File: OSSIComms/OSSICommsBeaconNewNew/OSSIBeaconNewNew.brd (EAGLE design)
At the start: 92 x 92 mm, 116 parts, among them Q1 NX-3215, U1 MAX890L, U10 MSP430F2132, U2 ADL5530, U3 NC7SZ04, U4 ADF7012, U5 OPA2347, U6 MAX890L, U7 MAX6369, U8 MCP1700_SOT23, U9 TPS3838, X1 ESQ-126-38-G-D, X2 RFCON-MCX-R/A, X3 5268-02, X4 JTAG10PINMINI-H, X5 5268-03, X7 P-PAD-S, X8 P-PAD-S

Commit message: beta 1 release
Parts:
- moved X6 2.54 mm to (88.9, 28.6)
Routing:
- net BEACON_SDA: track 58.6 -> 59.4 mm
- net BEACON_SCL: track 56.5 -> 57.3 mm
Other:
- outline, holes or cut-outs redrawn
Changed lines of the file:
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@@
 <setting verticaltext="up"/>
 </settings>
-<grid distance="1.27" unitdist="mm" unit="mm" style="lines" multiple="1" display="yes" altdistance="0.0125" altunitdist="inch" altunit="inch"/>
+<grid distance="1" unitdist="mm" unit="mm" style="lines" multiple="1" display="yes" altdistance="0.025" altunitdist="inch" altunit="inch"/>
 <layers>
 <layer number="1" name="Top" color="4" fill="1" visible="yes" active="yes"/>
@@
 <layer number="27" name="tValues" color="7" fill="1" visible="no" active="yes"/>
 <layer number="28" name="bValues" color="7" fill="1" visible="no" active="yes"/>
-<layer number="29" name="tStop" color="7" fill="3" visible="yes" active="yes"/>
+<layer number="29" name="tStop" color="7" fill="3" visible="no" active="yes"/>
 <layer number="30" name="bStop" color="7" fill="6" visible="no" active="yes"/>
 <layer number="31" name="tCream" color="7" fill="4" visible="no" active="yes"/>
@@
 <wire x1="3" y1="0" x2="89" y2="0" width="0" layer="20"/>
 <wire x1="89" y1="0" x2="92" y2="3" width="0" layer="20" curve="90"/>
-<wire x1="92" y1="3" x2="92" y2="89" width="0" layer="20"/>
+<wire x1="92" y1="3" x2="92" y2="36" width="0" layer="20"/>
+<wire x1="92" y1="56" x2="92" y2="89" width="0" layer="20"/>
 <wire x1="92" y1="89" x2="89" y2="92" width="0" layer="20" curve="90"/>
 <wire x1="79" y1="90" x2="79" y2="91" width="0" layer="20"/>
@@
 <wire x1="16" y1="87" x2="76" y2="87" width="0" layer="20"/>
 <wire x1="76" y1="87" x2="79" y2="90" width="0" layer="20" curve="90"/>
-<text x="89.535" y="39.6875" size="1.27" layer="1" font="vector" rot="R90">SDA</text>
-<text x="89.535" y="44.45" size="1.27" layer="1" font="vector" rot="R90">SCL</text>
-<text x="89.535" y="48.895" size="1.27" layer="1" font="vector" rot="R90">GND</text>
-<text x="89.535" y="48.895" size="1.27" layer="29" font="vector" rot="R90">GND</text>
-<text x="89.535" y="44.45" size="1.27" layer="29" font="vector" rot="R90">SCL</text>
-<text x="89.535" y="39.6875" size="1.27" layer="29" font="vector" rot="R90">SDA</text>
+<text x="89.535" y="13.0175" size="1.27" layer="1" font="vector" rot="R90">SDA</text>
+<text x="89.535" y="17.78" size="1.27" layer="1" font="vector" rot="R90">SCL</text>
+<text x="89.535" y="22.225" size="1.27" layer="1" font="vector" rot="R90">GND</text>
+<text x="89.535" y="22.225" size="1.27" layer="29" font="vector" rot="R90">GND</text>
+<text x="89.535" y="17.78" size="1.27" layer="29" font="vector" rot="R90">SCL</text>
+<text x="89.535" y="13.0175" size="1.27" layer="29" font="vector" rot="R90">SDA</text>
 <text x="11.43" y="71.12" size="1.778" layer="1" font="vector" rot="SR270">G.O.D.Sat</text>
 <text x="6.35" y="71.12" size="1.778" layer="1" font="vector" rot="SR270">CW Beacon</text>
@@
 <text x="29.21" y="55.245" size="1.27" layer="29" font="vector" rot="R90">P3.0</text>
 <text x="29.21" y="55.245" size="1.27" layer="1" font="vector" rot="R90">P3.0</text>
+<wire x1="90" y1="38" x2="88" y2="40" width="0" layer="20" curve="-90"/>
+<wire x1="88" y1="40" x2="88" y2="52" width="0" layer="20"/>
+<wire x1="88" y1="52" x2="90" y2="54" width="0" layer="20" curve="-90"/>
+<wire x1="92" y1="36" x2="92" y2="37" width="0" layer="20"/>
+<wire x1="92" y1="37" x2="91" y2="38" width="0" layer="20" curve="90"/>
+<wire x1="91" y1="38" x2="90" y2="38" width="0" layer="20"/>
+<wire x1="92" y1="56" x2="92" y2="55" width="0" layer="20"/>
+<wire x1="92" y1="55" x2="91" y2="54" width="0" layer="20" curve="-90"/>
+<wire x1="91" y1="54" x2="90" y2="54" width="0" layer="20"/>
 </plain>
 <attributes>
@@
 <element name="R27" library="OSSI" package="R0603(1608)" value="4.7k" x="59.69" y="43.18"/>
 <element name="R26" library="OSSI" package="R0603(1608)" value="4.7k" x="59.69" y="41.91"/>
-<element name="X6" library="OSSI" package="1X03" value="" x="88.9" y="31.115" rot="R90"/>
+<element name="X6" library="OSSI" package="1X03" value="" x="88.9" y="28.575" rot="R90"/>
 <element name="R39" library="OSSI" package="WSL1206" value="511" x="8.89" y="78.105" rot="R90"/>
 <element name="C43" library="OSSI" package="C0805(2012)" value="" x="6.35" y="78.105" rot="R270"/>
@@
 <vertex x="12.7" y="0"/>
 <vertex x="80.01" y="0"/>
-<vertex x="80.01" y="31.75"/>
+<vertex x="80.01" y="30.75"/>
+<vertex x="79.01" y="31.75"/>
 </polygon>
 <polygon width="0.254" layer="1" thermals="no">
@@
 <vertex x="77.47" y="13.335"/>
 <vertex x="77.47" y="31.75"/>
-<vertex x="80.3275" y="31.75"/>
+<vertex x="79.3275" y="31.75"/>
+<vertex x="80.3275" y="30.75"/>
 <vertex x="80.3275" y="0"/>
 <vertex x="12.7" y="0"/>
@@
 <wire x1="81.28" y1="33.48" x2="82.73" y2="32.03" width="0.4064" layer="16"/>
 <contactref element="X6" pad="2"/>
-<wire x1="86.6775" y1="33.3375" x2="84.1375" y2="33.3375" width="0.4064" layer="1"/>
+<wire x1="85.4075" y1="33.3375" x2="84.1375" y2="33.3375" width="0.4064" layer="1"/>
 <wire x1="84.1375" y1="33.3375" x2="82.8675" y2="32.0675" width="0.4064" layer="1"/>
 <wire x1="82.8675" y1="32.0675" x2="82.7675" y2="32.0675" width="0.4064" layer="1"/>
 <wire x1="82.7675" y1="32.0675" x2="82.73" y2="32.03" width="0.4064" layer="1"/>
-<wire x1="86.6775" y1="33.3375" x2="88.5825" y2="33.3375" width="0.4064" layer="1"/>
-<wire x1="88.5825" y1="33.3375" x2="88.9" y2="33.655" width="0.4064" layer="1"/>
+<wire x1="85.4075" y1="33.3375" x2="86.0425" y2="33.3375" width="0.4064" layer="1"/>
+<wire x1="86.0425" y1="33.3375" x2="87.63" y2="31.75" width="0.4064" layer="1"/>
+<wire x1="87.63" y1="31.75" x2="88.265" y2="31.115" width="0.4064" layer="1"/>
+<wire x1="88.265" y1="31.115" x2="88.9" y2="31.115" width="0.4064" layer="1"/>
 </signal>
 <signal name="BEACON_SDA">
@@
 <wire x1="82.73" y1="29.49" x2="82.83" y2="29.49" width="0.4064" layer="1"/>
 <wire x1="82.83" y1="29.49" x2="84.1375" y2="30.7975" width="0.4064" layer="1"/>
-<wire x1="84.1375" y1="30.7975" x2="88.5825" y2="30.7975" width="0.4064" layer="1"/>
-<wire x1="88.5825" y1="30.7975" x2="88.9" y2="31.115" width="0.4064" layer="1"/>
+<wire x1="84.1375" y1="30.7975" x2="86.0425" y2="30.7975" width="0.4064" layer="1"/>
+<wire x1="86.0425" y1="30.7975" x2="87.63" y2="29.21" width="0.4064" layer="1"/>
+<wire x1="87.63" y1="29.21" x2="88.265" y2="28.575" width="0.4064" layer="1"/>
+<wire x1="88.265" y1="28.575" x2="88.9" y2="28.575" width="0.4064" layer="1"/>
 </signal>
 <signal name="COMMS_SDA">

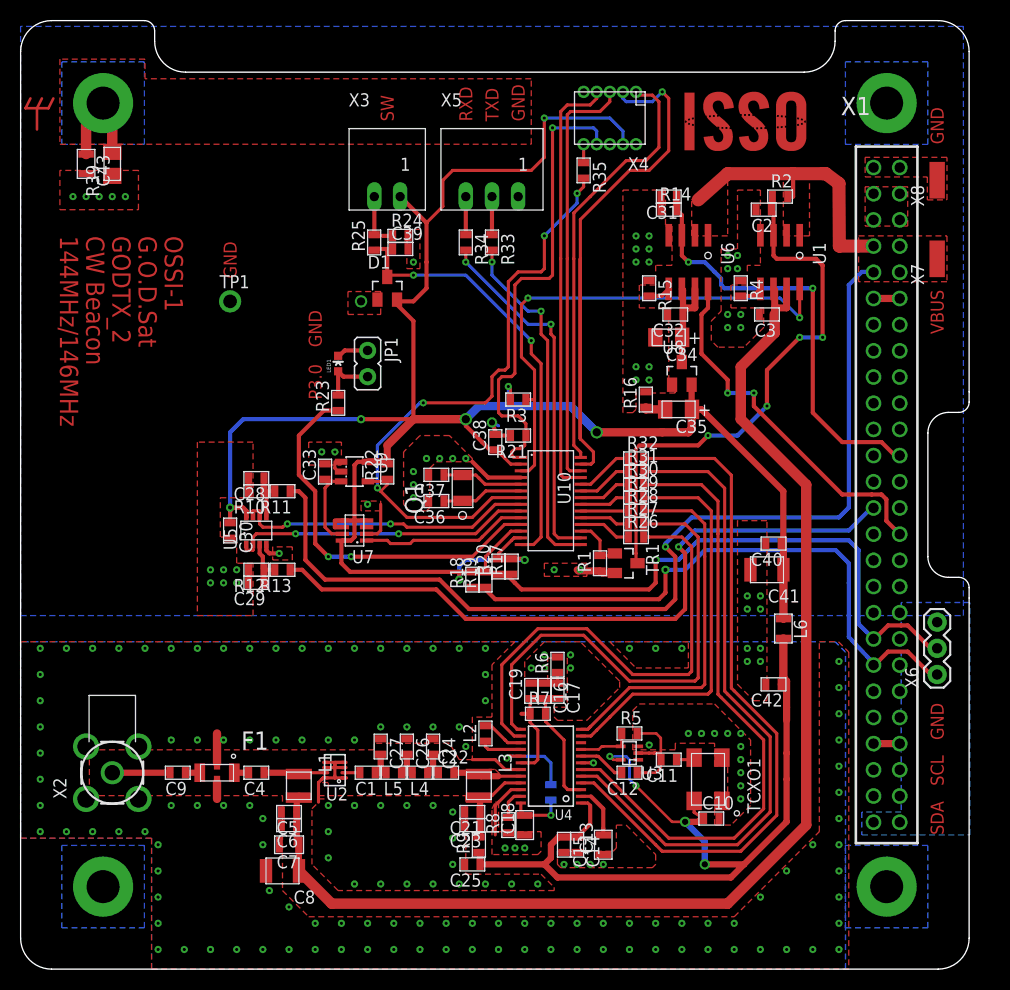
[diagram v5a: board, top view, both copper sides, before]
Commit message: schematics renumbered
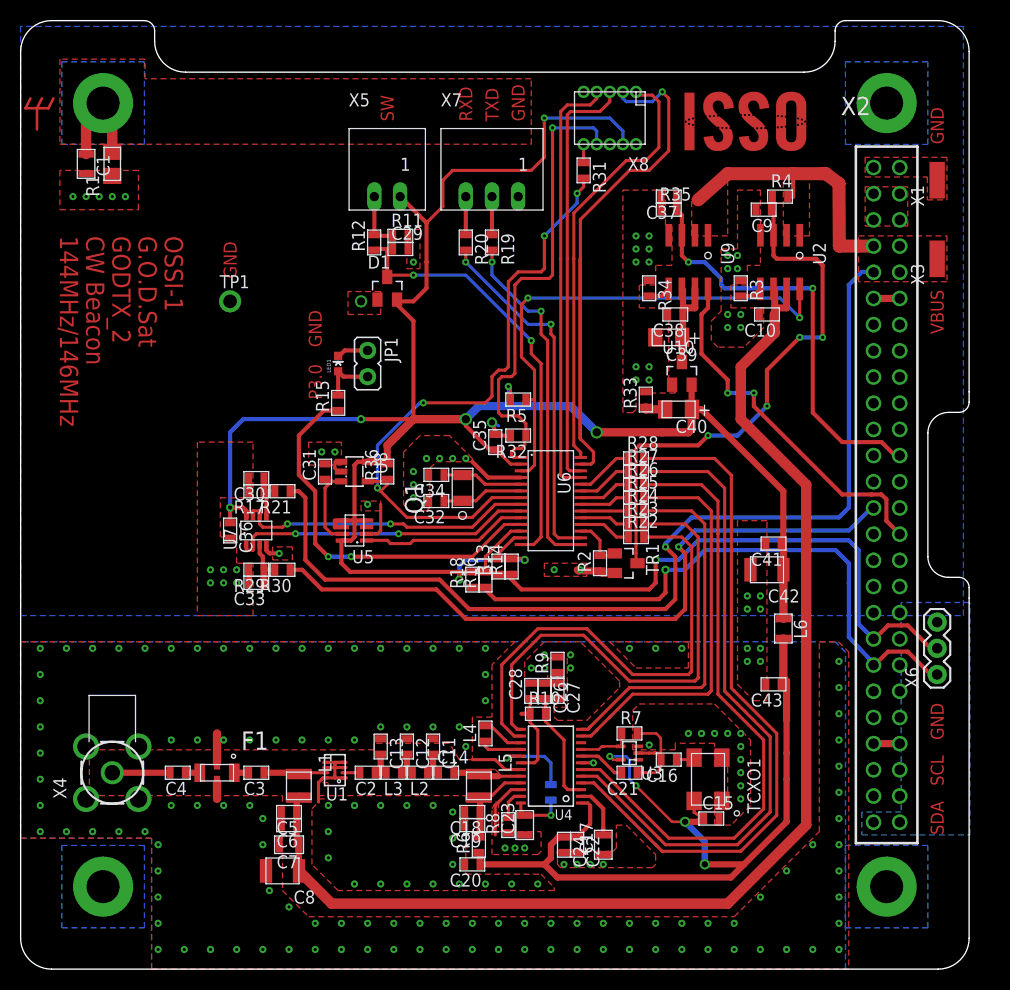
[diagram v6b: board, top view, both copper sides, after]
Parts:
- removed R39: 511, OSSI:WSL1206
- added R36: 100k, OSSI:R0603(1608)
- C1: value 10nF -> (none); device OSSI:C0603(1608) -> OSSI:C0805(2012)
- C10: value 10nF -> 100nF
- C11: value 1nF -> 22pF
- C12: value DNP -> 22pF
- C13: value 2.2uF, 0805 -> 22pF; device OSSI:C0805(2012) -> OSSI:C0603(1608)
- C14: value 100pF -> 1nF
- C15: value 1uF,0603 -> 10nF
- C16: value 68pF -> 1nF
- C17: value 1000pF -> 2.2uF, 0805; device OSSI:C0603(1608) -> OSSI:C0805(2012)
- C18: value 1uF 0805 -> 100pF; device OSSI:C0805(2012) -> OSSI:C0603(1608)
- C19: value 22pF -> 1uF
- C2: value 1uF -> 10nF
- C20: value 22nF -> (none)
- C21: value 100pF -> DNP
- C22: value 1nF -> 100pF
- C23: value 1uF -> 1uF 0805; device OSSI:C0603(1608) -> OSSI:C0805(2012)
- C24: value 22pF -> 1uF,0603
- C25: value (none) -> 22nF
- C26: value 22pF -> 68pF
- C27: value 22pF -> 1000pF
- C28: value TBD -> 22pF
- C29: value TBD -> 100nF
- C3: value 100nF -> 10nF
- C30, C33: value 100nF -> TBD
- C31: value 1uF -> 100nF
- C32: value 100nF -> 12.5pF
- C34: value 10uF, LDO Tantal 16V -> 12.5pF; device OSSI:C1206(3216)-A -> OSSI:C0603(1608)
- C35: value 10uF, LDO Tantal 16V -> 100nF; device OSSI:C1206(3216)-A -> OSSI:C0603(1608)
- C36: value 12.5pF -> 100nF
- C37: value 12.5pF -> 1uF
- C39: value 100nF -> 10uF, LDO Tantal 16V; device OSSI:C0603(1608) -> OSSI:C1206(3216)-A
- C4: value 10nF -> (none)
- C40: value 10nF -> 10uF, LDO Tantal 16V; device OSSI:C0603(1608) -> OSSI:C1206(3216)-A
- C41: value 22uF,1210 -> 10nF; device OSSI:C1210-GCM32 -> OSSI:C0603(1608)
- C42: value 100nF -> 22uF,1210; device OSSI:C0603(1608) -> OSSI:C1210-GCM32
- C43: value (none) -> 100nF; device OSSI:C0805(2012) -> OSSI:C0603(1608)
- C9: value (none) -> 1uF
- L2: value 10nH -> 68nH
- L3: value 470nH, 1008 size -> 68nH; device OSSI:L1008(2520) -> OSSI:L0603(1608)
- L4: value 68nH -> 10nH
- L5: value 68nH -> 470nH, 1008 size; device OSSI:L0603(1608) -> OSSI:L1008(2520)
- R1: value 100k -> 511; device OSSI:R0603(1608) -> OSSI:WSL1206
- R10: value 100k -> 5.1k
- R11: value 100k -> 47k
- R12, R22: value 100k -> 4.7k
- R13: value 100k -> 250
- R14: value 100k -> 10k
- R15: value 23.7k -> 1k
- R16: value 0 -> 250
- R17: value 10k -> 100k
- R19, R20: value 250 -> 4.7k
- R21, R29, R30, R35: value 4.7k -> 100k
- R23: value 1k -> 4.7k
- R24: value 47k -> 4.7k
- R3: value 100k -> 6.2k
- R33: value 4.7k -> 0
- R34: value 4.7k -> 23.7k
- R4: value 6.2k -> 100k
- R5: value 1M -> 100k
- R6: value 2.4k -> 0
- R7: value 5.1k -> 1M
- R9: value 0 -> 2.4k
- U1: value MAX890L -> ADL5530; device OSSI:SO8 -> OSSI:LFCSP8_CP
- U10: value MSP430F2132 -> MCP1700_SOT23; device OSSI:PW28 -> OSSI:SOT23
- U2: value ADL5530 -> MAX890L; device OSSI:LFCSP8_CP -> OSSI:SO8
- U5: value OPA2347 -> MAX6369; device OSSI:SOT23-8DCN -> OSSI:SOT23-8
- U6: value MAX890L -> MSP430F2132; device OSSI:SO8 -> OSSI:PW28
- U7: value MAX6369 -> OPA2347; device OSSI:SOT23-8 -> OSSI:SOT23-8DCN
- U8: value MCP1700_SOT23 -> TPS3838; device OSSI:SOT23 -> OSSI:SOT23-5DBV
- U9: value TPS3838 -> MAX890L; device OSSI:SOT23-5DBV -> OSSI:SO8
- X1: value ESQ-126-38-G-D -> P-PAD-S; device OSSI:ESQ-126-XX-X-D -> OSSI:P-PAD-S
- X2: value RFCON-MCX-R/A -> ESQ-126-38-G-D; device OSSI:MCX-R/A -> OSSI:ESQ-126-XX-X-D
- X3: value 5268-02 -> P-PAD-S; device OSSI:5628-02 -> OSSI:P-PAD-S
- X4: value JTAG10PINMINI-H -> RFCON-MCX-R/A; device OSSI:M50-3200545 -> OSSI:MCX-R/A
- X5: value 5268-03 -> 5268-02; device OSSI:5268-03 -> OSSI:5628-02
- X7: value P-PAD-S -> 5268-03; device OSSI:P-PAD-S -> OSSI:5268-03
- X8: value P-PAD-S -> JTAG10PINMINI-H; device OSSI:P-PAD-S -> OSSI:M50-3200545
- moved C43 83.6 mm to (73.0, 27.6), turned to 180 degrees
- moved X2 79.8 mm to (84.0, 46.0), turned to 0 degrees
- moved X4 79.8 mm to (8.89, 19.1), turned to 90 degrees
- moved C9 78.8 mm to (72.1, 73.7)
- moved C2 66.8 mm to (33.7, 19.1)
- moved C3 66.6 mm to (22.9, 19.1)
- moved U1 65.5 mm to (30.5, 19.3)
- moved U2 65.5 mm to (73.7, 68.6)
- moved C1 65.1 mm to (6.35, 78.1), turned to 270 degrees
- moved R1 61.1 mm to (8.89, 78.1)
- moved X3 53.7 mm to (88.9, 68.9), turned to 90 degrees
- moved C10 49.2 mm to (72.4, 63.5), turned to 180 degrees
- moved X7 43.6 mm to (45.7, 74.9), turned to 0 degrees
- moved C31 42.7 mm to (29.5, 48.3), turned to 90 degrees
- moved R2 39.6 mm to (56.2, 39.4), turned to 90 degrees
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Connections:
- net 3.3VBEACON: now also C36.1, C41.1, C42.P$1, R14.2, R36.2, R5.2, U5.4, U5.5, U5.6, U6.2, U8.5, X5.1, X8.4; no longer C30.1, C38.1, C41.P$1, R17.2, R22.2, R3.2, U7.4, U7.5, U7.6, U8.2, U9.5, X3.1, X4.4
- net 3.3VOBC: now also X2.45, X2.46; no longer X1.45, X1.46
- net ADC0: now also U6.8, U7.6, U7.7; no longer U10.8, U5.6, U5.7
- net ADC1: now also U6.9, U7.1, U7.2; no longer U10.9, U5.1, U5.2
- net ANT_DEPLOY1: now also X2.19; no longer X1.19
- net ANT_DEPLOY2: now also X2.20; no longer X1.20
- net BAT_-CHRG: now also X2.42; no longer X1.42
- net BAT_-FAULT: now also X2.44; no longer X1.44
- net BAT_-ON: now also X2.38; no longer X1.38
- net BAT_TEMP: now also X2.47; no longer X1.47
- net BEACON_-FAULT: now also U9.8, X2.30; no longer U6.8, X1.30
- net BEACON_CE: now also R22.2; no longer R26.2
- net BEACON_CWCONTROL: now also R11.1, R12.2, X5.2; no longer R24.1, R25.2, X3.2
- net BEACON_DATA: now also R28.2; no longer R32.2
- net BEACON_MUXOUT: now also R26.2; no longer R30.2
- net BEACON_OFF: now also C37.1, R35.2, U9.3, X2.24; no longer C31.1, R14.2, U6.3, X1.24
- net BEACON_RFOUT: now also C13.2, C2.1, L3.2; no longer C1.1, C27.2, L5.2
- net BEACON_SCL: now also R13.1, R14.1, X2.37; no longer R17.1, R20.1, X1.37
- net BEACON_SCLK: now also R25.2; no longer R29.2
- net BEACON_SDA: now also R16.1, X2.39; no longer R19.1, X1.39
- net BEACON_SDATA: now also R24.2; no longer R28.2
- net BEACON_SLE: now also R23.2; no longer R27.2
- net BEACON_TXCLK: now also R27.2; no longer R31.2
- net BEACON_WDT_RST: now also C31.1, U5.7, U8.3; no longer C33.1, U7.7, U9.3
- net BUS_CS: now also R30.1, X2.27; no longer R13.1, X1.27
- net COMMS_-FAULT: now also X2.32; no longer X1.32
- net COMMS_OFF: now also X2.25; no longer X1.25
- net COMMS_SCL: now also X2.41; no longer X1.41
- net COMMS_SDA: now also X2.43; no longer X1.43
- net GND: now also C1.2, C11.1, C12.1, C17.1, C18.2, C20.2, C22.2, C23.1, C24.2, C35.2, C41.2, C42.P$2, C9.2, R1.P$1, R11.2, R17.2, R2.1, R29.2, R3.1, R32.2, R33.2, R34.1, R35.1, R9.2, U1.1, U1.3, U1.5, U1.6, U1.8, U10.1, U5.2, U7.4, U8.2, U9.4, X2.1, X2.51, X2.52, X4.2, X4.3, X4.4, X4.5, X7.1, X8.9; no longer C14.2, C16.1, C18.1, C2.2, C21.2, C23.2, C24.1, C25.2, C27.1, C3.2, C40.2, C41.P$2, C42.2, R1.1, R10.2, R12.2, R14.1, R15.1, R16.2, R21.2, R24.2, R39.P$1, R4.1, R6.2, U10.4, U2.1, U2.3, U2.5, U2.6, U2.8, U5.4, U7.2, U9.1, U9.2, X1.2, X1.51, X1.52, X2.3, X2.4, X2.5, X4.9, X5.1, X8.1
- net LED_-FAULT: now also X2.28; no longer X1.28
- net LED_OFF: now also X2.23; no longer X1.23
- net LED_SCL: now also X2.33; no longer X1.33
- net LED_SDA: now also X2.35; no longer X1.35
- net N$1: now also R15.1, U6.11; no longer R23.1, U10.11
- net N$10: now also R13.2, U6.13; no longer R20.2, U10.13
- net N$11: now also R20.2, U6.16; no longer R34.2, U10.16
- net N$12: now also U5.1, U6.10; no longer U10.10, U7.1
- net N$13: now also C29.1, R12.1, U6.14; no longer C39.1, R25.1, U10.14
- net N$14: now also L4.1; no longer L2.1
- net N$15: now also L4.2; no longer L2.2
- net N$16: now also C23.2, C25.1; no longer C18.2, C20.1
- net N$17: now also C25.2; no longer C20.2
- net N$19: now also C9.1, R4.1, U2.3; no longer C2.1, R2.1, U1.3
- net N$2: now also U6.27, X8.3; no longer U10.27, X4.3
- net N$20: now also C27.1, R9.1; no longer C17.1, R6.1
- net N$21: now also R3.2, U2.5; no longer R4.2, U1.5
- net N$22: now also C30.1, R17.1, R21.2, U7.5; no longer C28.1, R10.1, R11.2, U5.5
- net N$23: now also C14.2, L5.P$2; no longer C22.2, L3.P$2
- net N$24: now also C28.1, R10.1; no longer C19.1, R7.1
- net N$25: now also C17.2; no longer C13.2
- net N$26: now also C26.2, C27.2, R10.2; no longer C16.2, C17.2, R7.2
- net N$27: now also C18.1, C19.1, L5.P$1, R6.2; no longer C21.1, C23.1, L3.P$1, R9.2
- net N$28: now also C2.2, U1.2; no longer C1.2, U2.2
- net N$29: now also C11.2, C14.1, L2.1; no longer C22.1, C24.2, L4.1
- net N$3: now also U6.26, X8.5; no longer U10.26, X4.5
- net N$30: now also C3.1, U1.7; no longer C4.1, U2.7
- net N$31: now also R31.1, X8.10; no longer R35.1, X4.10
- net N$32: now also R34.2, U9.5; no longer R15.2, U6.5
- net N$33: now also C33.1, R29.1, R30.2, U7.3; no longer C29.1, R12.1, R13.2, U5.3
- net N$34: now also C3.2; no longer C4.2
- net N$35: now also C4.1; no longer C9.1
- net N$36: now also C12.2, L2.2, L3.1; no longer C26.2, L4.2, L5.1
- net N$37: now also C4.2, X4.1; no longer C9.2, X2.1
- net N$38: now also C16.2, C21.1, R7.2; no longer C11.2, C12.1, R5.2
- net N$39: now also R19.2, U6.15; no longer R33.2, U10.15
- net N$4: now also U6.25, X8.7; no longer U10.25, X4.7
- net N$40: now also C40.2, R33.1; no longer C35.2, R16.1
- net N$41: now also R28.1, U6.24; no longer R32.1, U10.24
- net N$42: now also R27.1, U6.23; no longer R31.1, U10.23
- net N$43: now also R26.1, U6.22; no longer R30.1, U10.22
- net N$44: now also R25.1, U6.21; no longer R29.1, U10.21
- net N$45: now also R24.1, U6.20; no longer R28.1, U10.20
- net N$46: now also R23.1, U6.19; no longer R27.1, U10.19
- net N$47: now also R22.1, U6.18; no longer R26.1, U10.18
- net N$5: now also C34.1, U6.5; no longer C37.1, U10.5
- net N$6: now also C32.1, U6.6; no longer C36.1, U10.6
- net N$666: now also C38.1, C39.1, U10.3, U9.6, U9.7; no longer C32.1, C34.1, U6.6, U6.7, U8.3
- net N$69: now also C16.1; no longer C11.1
- net N$7: now also R15.2; no longer R23.2
- net N$8: now also U6.28, X8.1; no longer U10.28, X4.1
- net N$9: now also R16.2, U6.12; no longer R19.2, U10.12
- net OBC_-FAULT: now also X2.34; no longer X1.34
- net OBC_OFF: now also X2.26; no longer X1.26
- net OSC1: now also C21.2; no longer C12.2
- net OSC2: now also R7.1; no longer R5.1
- net PANELTEMP_SCL: now also X2.29; no longer X1.29
- net PANELTEMP_SDA: now also X2.31; no longer X1.31
- net PA_-FAULT: now also R5.1, U2.8, U6.3; no longer R3.1, U1.8, U10.3
- net PA_ON: now also R2.2, U6.17; no longer R1.2, U10.17
- net RESETBEACON: now also R31.2, R36.1, U6.7, U8.4; no longer R22.1, R35.2, U10.7, U9.4
- net RXD: now also R20.1, X7.3; no longer R34.1, X5.3
- net SCCHG_EN: now also X2.21; no longer X1.21
- net SCOUT_-PG: now also X2.50; no longer X1.50
- net SCOUT_EN: now also X2.22; no longer X1.22
- net SC_-ON: now also X2.40; no longer X1.40
- net SC_-PFO: now also X2.48; no longer X1.48
- net SOLAR_-ON: now also X2.36; no longer X1.36
- net SOLAR_CS1: now also X2.15; no longer X1.15
- net SOLAR_CS2: now also X2.14; no longer X1.14
- net SOLAR_CS3: now also X2.17; no longer X1.17
- net SOLAR_CS4: now also X2.16; no longer X1.16
- net SOLAR_CS5: now also X2.18; no longer X1.18
- net STRUT_GND: now also C1.1, R1.P$2; no longer C43.1, R39.P$2
- net SUPERCAP_TEMP: now also X2.49; no longer X1.49
- net TEST: now also R32.1, U6.1, X8.8; no longer R21.1, U10.1, X4.8
- net TXD: now also R19.1, X7.2; no longer R33.1, X5.2
- net VBAT: now also X2.11, X2.12; no longer X1.11, X1.12
- net VBEACON_PA: now also C10.1, U2.6, U2.7; no longer C3.1, U1.6, U1.7
- net VBUS: now also R21.1, R4.2, U2.1, U2.2, U9.1, U9.2, X2.10, X2.7, X2.8, X2.9, X3.1; no longer R11.1, R2.2, U1.1, U1.2, U6.1, U6.2, X1.10, X1.7, X1.8, X1.9, X7.1
- net VCCRF: now also C20.1, C22.1, C24.1, C43.1, R6.1; no longer C10.1, C14.1, C25.1, C42.1, R9.1
- net VSOLAR: now also X2.3, X2.4, X2.5, X2.6; no longer X1.3, X1.4, X1.5, X1.6
- net VSUPERCAP: now also X2.13; no longer X1.13

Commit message: beacon valued corrected
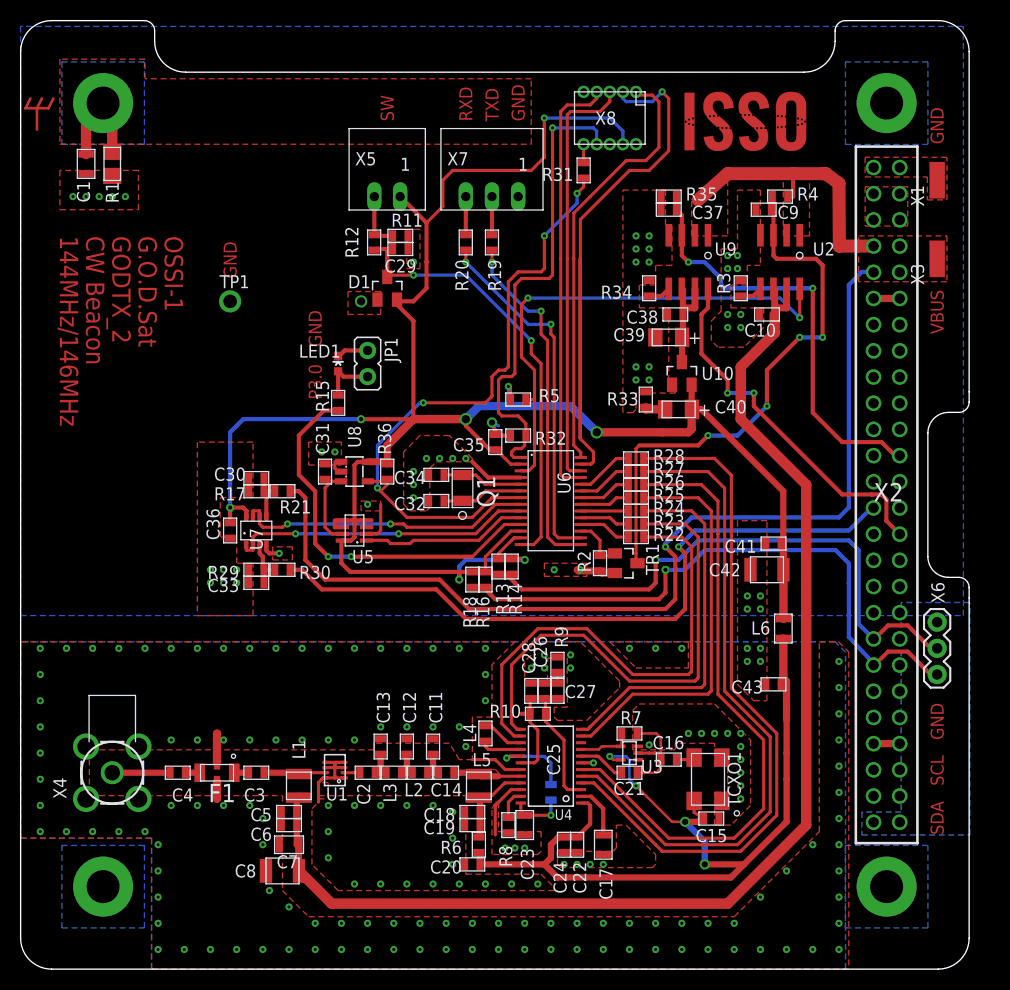
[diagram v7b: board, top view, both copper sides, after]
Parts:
- C12: value 22pF -> 39pF
- C20: value (none) -> 1uF,0603 Too Small!!
- C4: value (none) -> 10nF
- L6: value 5~15R ferrite bead -> 7 R Ferrite Bead, 3A
- R29: value 100k -> DNP
- R30: value 100k -> 10k
- R32: value 4.7k -> 100k

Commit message: beacon value changed
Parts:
- C4: value 10nF -> 100pF
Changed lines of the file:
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@@
 <attribute name="VALUE" x="24.050003125" y="25.050003125" size="1.778" layer="27" rot="R180"/>
 </element>
-<element name="C4" library="OSSI" package="C0603(1608)" value="10nF" x="15.24" y="19.05" smashed="yes" rot="R180">
+<element name="C4" library="OSSI" package="C0603(1608)" value="100pF" x="15.24" y="19.05" smashed="yes" rot="R180">
 <attribute name="NAME" x="16.764" y="17.526" size="1.27" layer="25" font="vector" rot="R180"/>
 <attribute name="VALUE" x="16.129" y="21.082" size="1.27" layer="27" rot="R180"/>
